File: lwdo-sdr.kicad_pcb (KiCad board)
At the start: 2 copper layers, 162 x 120 mm, 359 parts, among them J101 IN1, J102 IN2, J103 IN3, J104 IN4, J105 USB_B, J106 CLK_OUT, J107 REF_IN, J1401 Conn_02x10_Odd_Even, Q1201 NX7002AK, Q1202 PMN48XP, U1001 74LVC1G157, U1002 74LVC2G04, U1101 74LVC2GU04, U1102 74LVC2G04, U1201 TL431AFDT, U1202 TL431AFDT, U1203 TL431AFDT, U1204 MCP1824T-330, U1205 NCV8164ASN120T1G, U1206 MCP1824T-330, U1207 NCV8164ASN250T1G, U1208 NCV8164ASN330T1G, U1301 AT93C56, U1302 FT2232HL, U1401 74AVC4T245PW, U1402 74AVC4T245PW, U201 ICE40HX4K, U202 W25Q16JV, U203 IS61WV25616FBLL-10TLI, U301 THS4521ID, U401 THS4521ID, U501 THS4521ID, U601 THS4521ID, U701 AD7357xRU, U801 AD7357xRU, U901 DAC8551, U902 MCP1501-33xSN, U903 NCS325, U904 74LVC2GU04, U905 74LVC2G04, X901 DOT050V-020.0M, Y1301 12MHz CL=18p

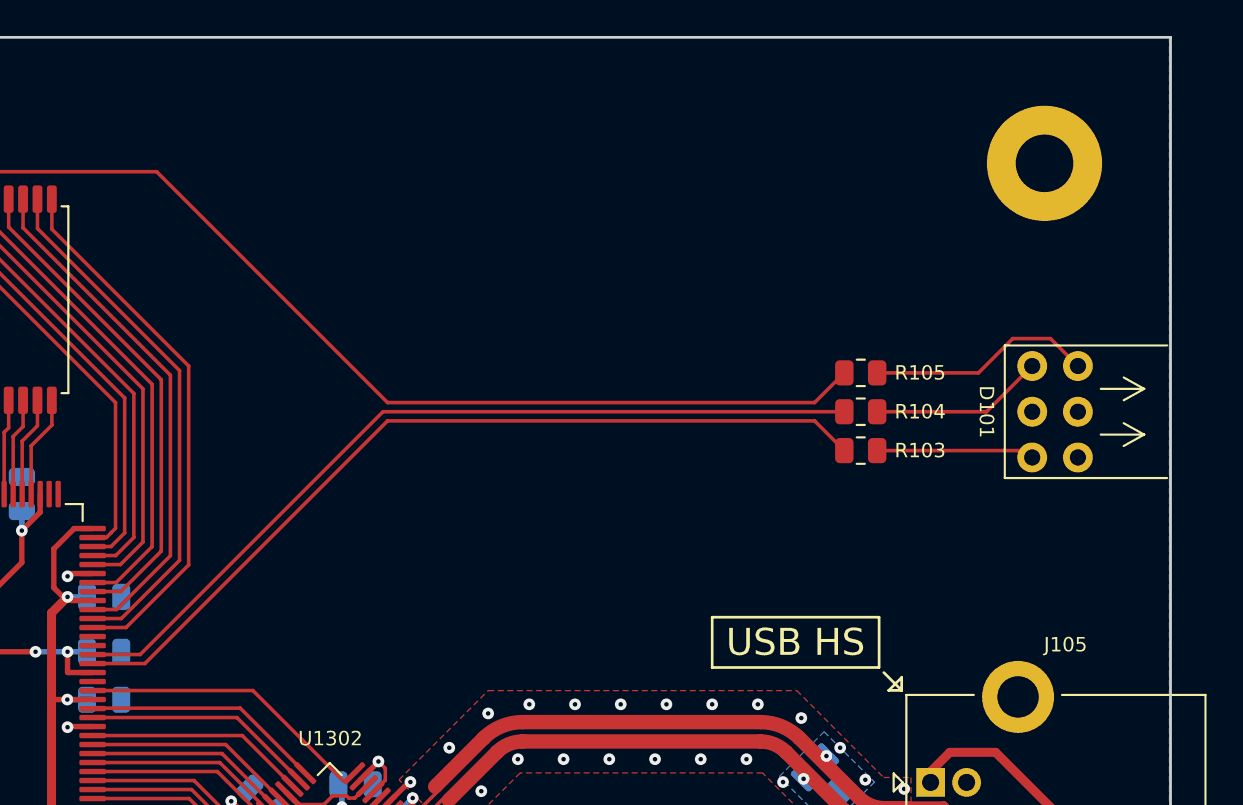
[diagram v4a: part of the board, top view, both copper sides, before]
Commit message: PCB: add silkscreen artwork + revision - Artwork by https://twitter.com/onisarashi/status/1423701946305847296
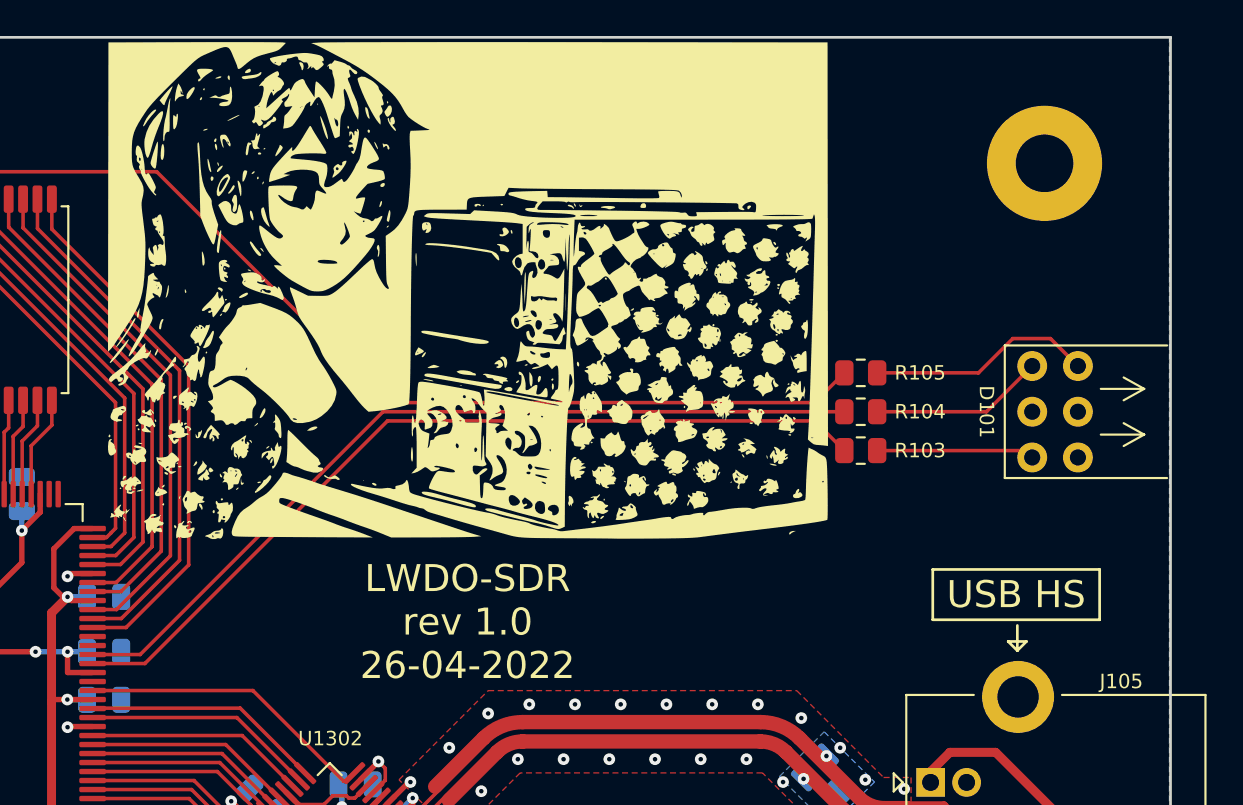
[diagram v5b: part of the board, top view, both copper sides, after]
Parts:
- added G***: LOGO, LOGO, F.Cu at (202.9, 44.1)
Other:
- board text added: "LWDO-SDR rev 1.0 26-04-2022"
